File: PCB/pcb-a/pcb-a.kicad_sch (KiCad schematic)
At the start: 12 parts, among them Q3 BC337, SW1 config, U1 ESP32-S2-DevKitM

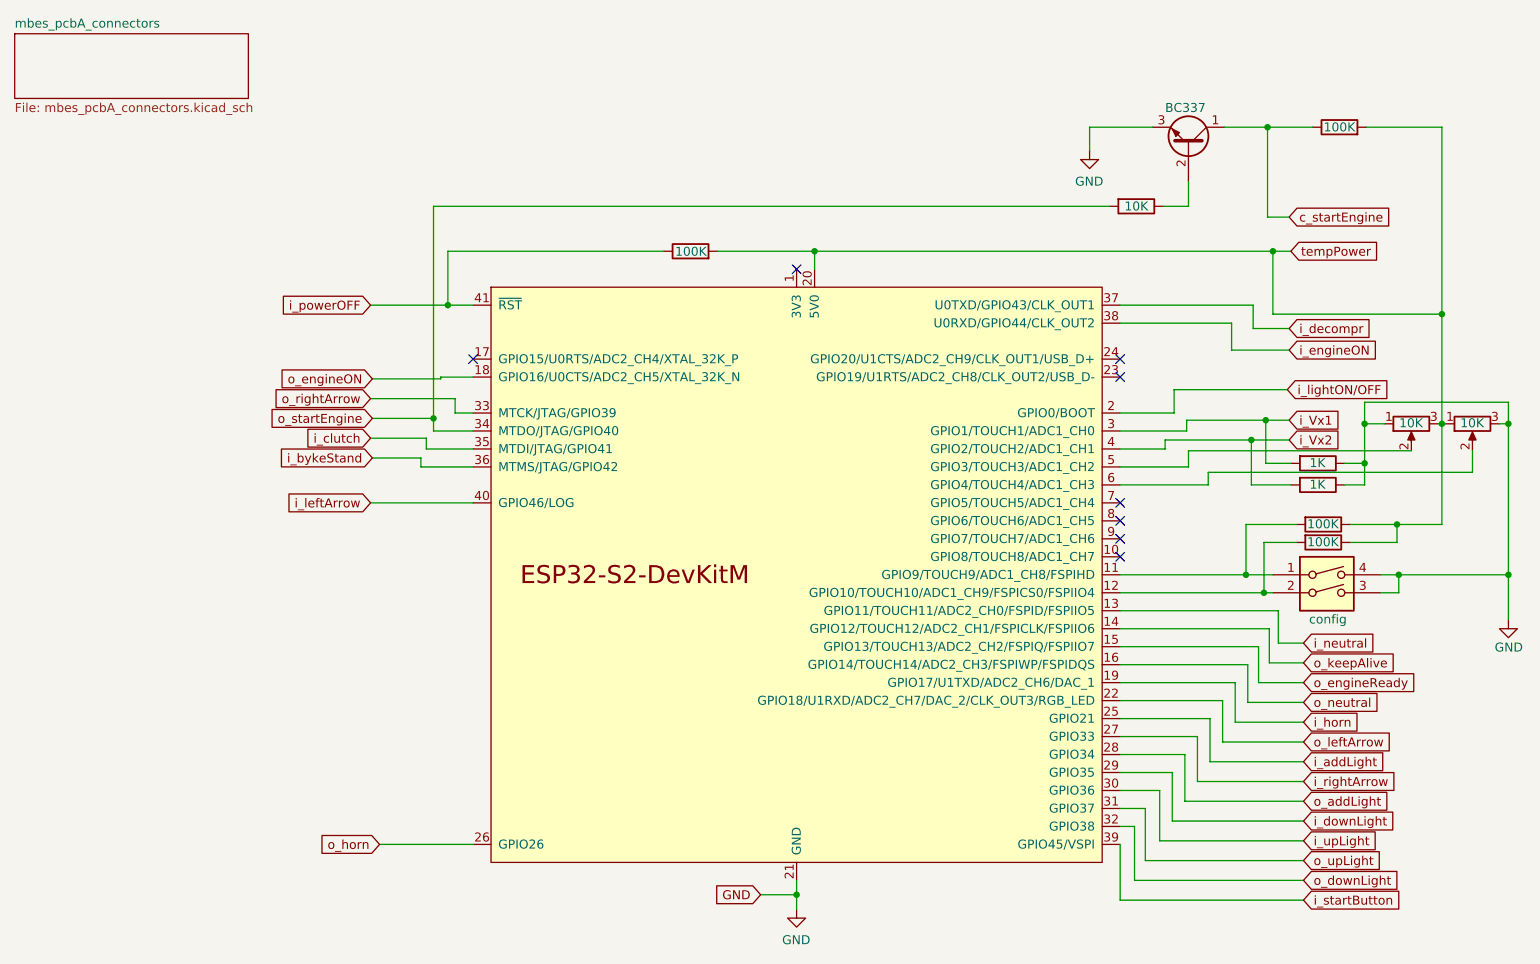
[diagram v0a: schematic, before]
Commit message: Fixes and updates
This version will be tested soon. It is fully implemented with THT devices using ESP32-S2 DevKit
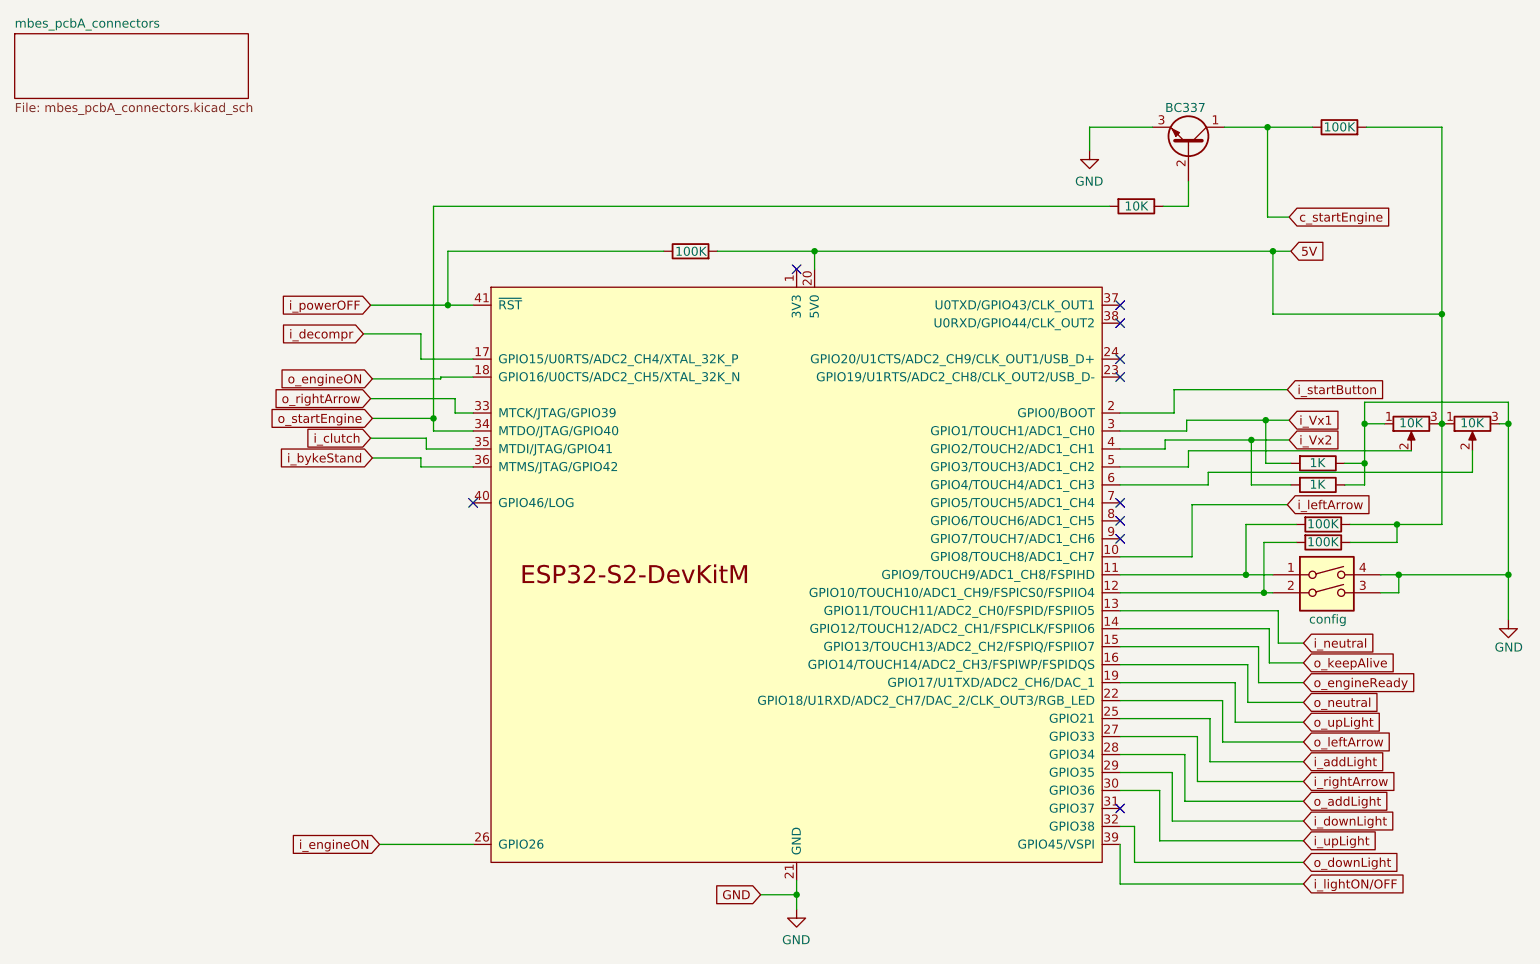
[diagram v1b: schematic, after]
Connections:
- net i_horn is gone; now on net o_upLight: U1.19 (GPIO17/U1TXD/ADC2_CH6/DAC_1)
- net o_horn is gone; now on net i_engineON: U1.26 (GPIO26)
- net i_decompr: now also U1.17 (GPIO15/U0RTS/ADC2_CH4/XTAL_32K_P); no longer U1.37 (U0TXD/GPIO43/CLK_OUT1)
- net i_engineON: no longer U1.38 (U0RXD/GPIO44/CLK_OUT2)
- net i_leftArrow: now also U1.10 (GPIO8/TOUCH8/ADC1_CH7); no longer U1.40 (GPIO46/LOG)
- net i_lightON/OFF: now also U1.39 (GPIO45/VSPI); no longer U1.2 (GPIO0/BOOT)
- net i_startButton: now also U1.2 (GPIO0/BOOT); no longer U1.39 (GPIO45/VSPI)
- net o_upLight: no longer U1.31 (GPIO37)
- net tempPower renamed 5V
- no-connect marks 8 -> 10

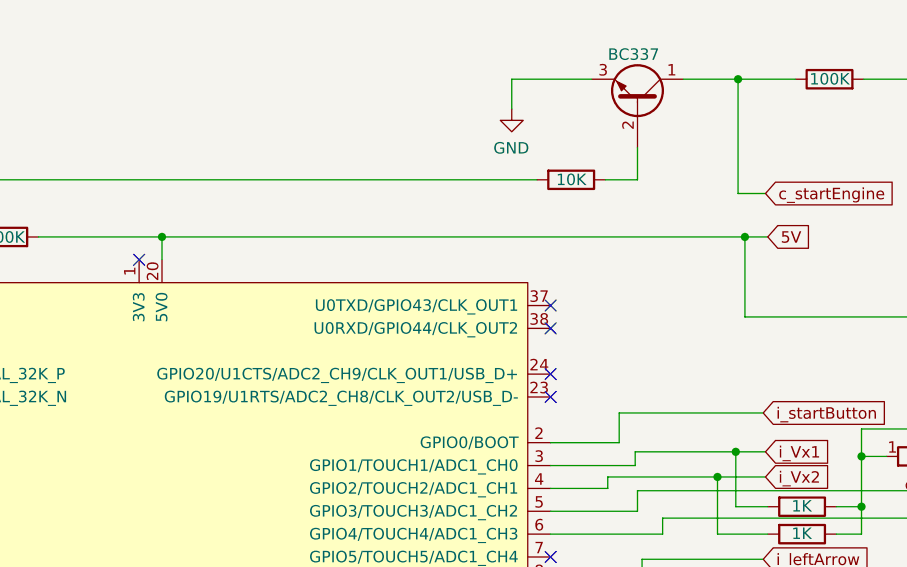
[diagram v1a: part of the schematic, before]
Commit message: Changes to reduce PCB size
- The resistors type has been changed from THT to SMD
- Configuration switches has been moved to fit PCB space in better way
- An electrolitic capicitor has been added
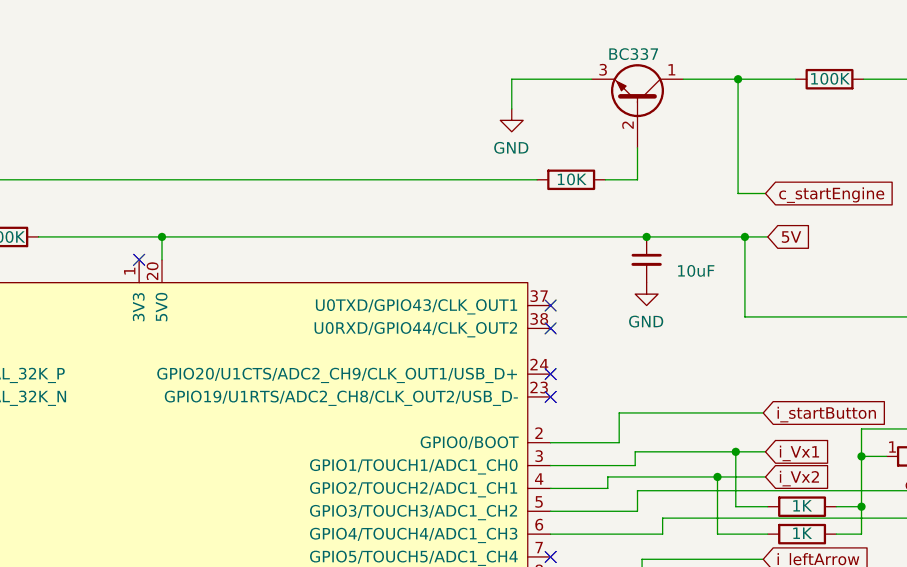
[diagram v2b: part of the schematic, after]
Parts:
- added C1: 10uF, Capacitor_THT:CP_Radial_D6.3mm_P2.50mm, symbol Device:C_Small
- R2, R3, R4, R5, R6, R7, R8: footprint Resistor_THT:R_Axial_DIN0204_L3.6mm_D1.6mm_P5.08mm_Horizontal -> Resistor_SMD:R_1206_3216Metric
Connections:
- net 5V: now also C1.1
- net GND: now also C1.2
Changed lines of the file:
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@@
 	)
 	(junction
+		(at 188.976 50.8)
+		(diameter 0)
+		(color 0 0 0 0)
+	)
+	(junction
 		(at 217.424 89.408)
 		(diameter 0)
@@
 	(wire
 		(pts
+			(xy 188.976 50.8) (xy 135.128 50.8)
+		)
+		(stroke
+			(width 0)
+			(type default)
+		)
+	)
+	(wire
+		(pts
 			(xy 199.39 104.14) (xy 178.308 104.14)
 		)
@@
 	(wire
 		(pts
-			(xy 199.898 50.8) (xy 135.128 50.8)
+			(xy 199.898 50.8) (xy 188.976 50.8)
 		)
 		(stroke
@@
 			)
 		)
-		(property "Footprint" "Resistor_THT:R_Axial_DIN0204_L3.6mm_D1.6mm_P5.08mm_Horizontal"
+		(property "Footprint" "Resistor_SMD:R_1206_3216Metric"
 			(at 206.248 82.042 90)
 			(effects
@@
 			)
 		)
-		(property "Footprint" "Resistor_THT:R_Axial_DIN0204_L3.6mm_D1.6mm_P5.08mm_Horizontal"
+		(property "Footprint" "Resistor_SMD:R_1206_3216Metric"
 			(at 206.248 78.994 90)
 			(effects
@@
 			)
 		)
-		(property "Footprint" "Resistor_THT:R_Axial_DIN0204_L3.6mm_D1.6mm_P5.08mm_Horizontal"
+		(property "Footprint" "Resistor_SMD:R_1206_3216Metric"
 			(at 207.01 87.63 90)
 			(effects
@@
 			)
 		)
-		(property "Footprint" "Resistor_THT:R_Axial_DIN0204_L3.6mm_D1.6mm_P5.08mm_Horizontal"
+		(property "Footprint" "Resistor_SMD:R_1206_3216Metric"
 			(at 207.01 90.17 90)
 			(effects
@@
 	)
 	(symbol
+		(lib_id "Device:C_Small")
+		(at 188.976 53.34 0)
+		(unit 1)
+		(exclude_from_sim no)
+		(in_bom yes)
+		(on_board yes)
+		(dnp no)
+		(fields_autoplaced yes)
+		(property "Reference" "C1"
+			(at 192.278 52.0762 0)
+			(effects
+				(font
+					(size 1.27 1.27)
+				)
+				(justify left)
+				(hide yes)
+			)
+		)
+		(property "Value" "10uF"
+			(at 192.278 54.6162 0)
+			(effects
+				(font
+					(size 1.27 1.27)
+				)
+				(justify left)
+			)
+		)
+		(property "Footprint" "Capacitor_THT:CP_Radial_D6.3mm_P2.50mm"
+			(at 188.976 53.34 0)
+			(effects
+				(font
+					(size 1.27 1.27)
+				)
+				(hide yes)
+			)
+		)
+		(property "Datasheet" "~"
+			(at 188.976 53.34 0)
+			(effects
+				(font
+					(size 1.27 1.27)
+				)
+				(hide yes)
+			)
+		)
+		(property "Description" "Unpolarized capacitor, small symbol"
+			(at 188.976 53.34 0)
+			(effects
+				(font
+					(size 1.27 1.27)
+				)
+				(hide yes)
+			)
+		)
+		(pin "2"
+		)
+		(pin "1"
+		)
+		(instances
+			(project ""
+				(path "/709d0967-afe5-49d3-92a5-d2bb94550bdb"
+					(reference "C1")
+					(unit 1)
+				)
+			)
+		)
+	)
+	(symbol
 		(lib_id "power:GND")
 		(at 173.99 36.576 0)
@@
 			)
 		)
-		(property "Footprint" "Resistor_THT:R_Axial_DIN0204_L3.6mm_D1.6mm_P5.08mm_Horizontal"
+		(property "Footprint" "Resistor_SMD:R_1206_3216Metric"
 			(at 180.594 42.672 90)
 			(effects
@@
 			)
 		)
-		(property "Footprint" "Resistor_THT:R_Axial_DIN0204_L3.6mm_D1.6mm_P5.08mm_Horizontal"
+		(property "Footprint" "Resistor_SMD:R_1206_3216Metric"
 			(at 117.602 52.578 90)
 			(effects
@@
 			)
 		)
-		(property "Footprint" "Resistor_THT:R_Axial_DIN0204_L3.6mm_D1.6mm_P5.08mm_Horizontal"
+		(property "Footprint" "Resistor_SMD:R_1206_3216Metric"
 			(at 209.296 35.052 90)
 			(effects
@@
 					(unit 1)
 				)
+			)
+		)
+	)
+	(symbol
+		(lib_id "power:GND")
+		(at 188.976 55.88 0)
+		(unit 1)
+		(exclude_from_sim no)
+		(in_bom yes)
+		(on_board yes)
+		(dnp no)
+		(property "Reference" "#PWR02"
+			(at 188.976 62.23 0)
+			(effects
+				(font
+					(size 1.27 1.27)
+				)
+				(hide yes)
+			)
+		)
+		(property "Value" "GND"
+			(at 188.9252 60.2488 0)
+			(effects
+				(font
+					(size 1.27 1.27)
+				)
+			)
+		)
+		(property "Footprint" ""
+			(at 188.976 55.88 0)
+			(effects
+				(font
+					(size 1.27 1.27)
+				)
+				(hide yes)
+			)
+		)
+		(property "Datasheet" ""
+			(at 188.976 55.88 0)
+			(effects
+				(font
+					(size 1.27 1.27)
+				)
+				(hide yes)
+			)
+		)
+		(property "Description" ""
+			(at 188.976 55.88 0)
+			(effects
+				(font
+					(size 1.27 1.27)
+				)
+				(hide yes)
+			)
+		)
+		(pin "1"
+		)
+		(instances
+			(project "pcb-a"
+				(path "/709d0967-afe5-49d3-92a5-d2bb94550bdb"
+					(reference "#PWR02")
+					(unit 1)
+				)

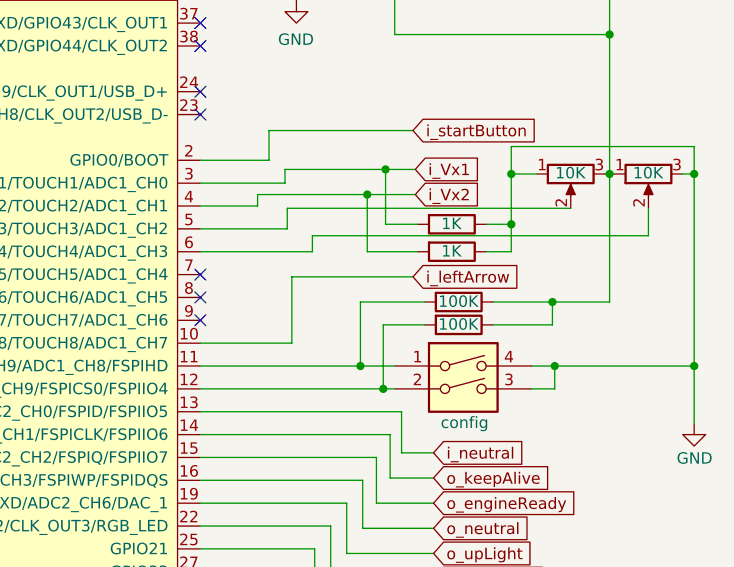
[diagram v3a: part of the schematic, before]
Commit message: hanges and fix
- The R6 and R8 pull-up resistors have been removed. I will use internal ones
- The J2 connector position has been moved
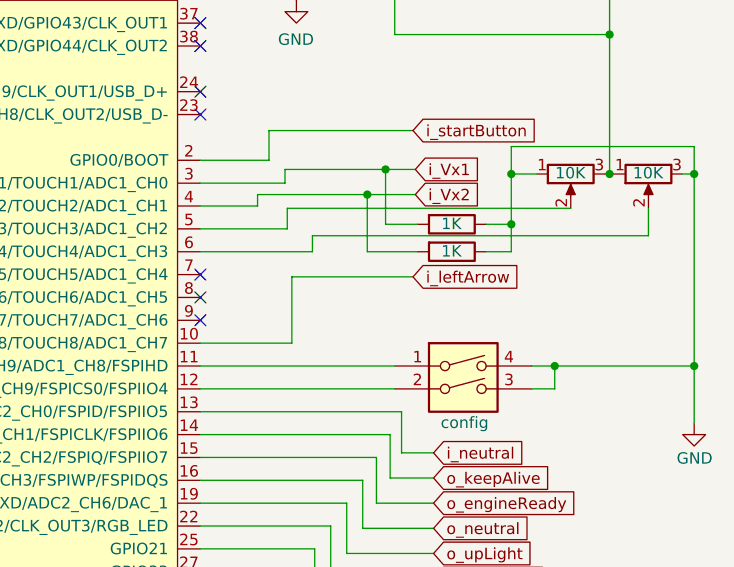
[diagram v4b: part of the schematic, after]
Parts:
- removed R5, R8: 100K, Resistor_SMD:R_1206_3216Metric, symbol Device:R

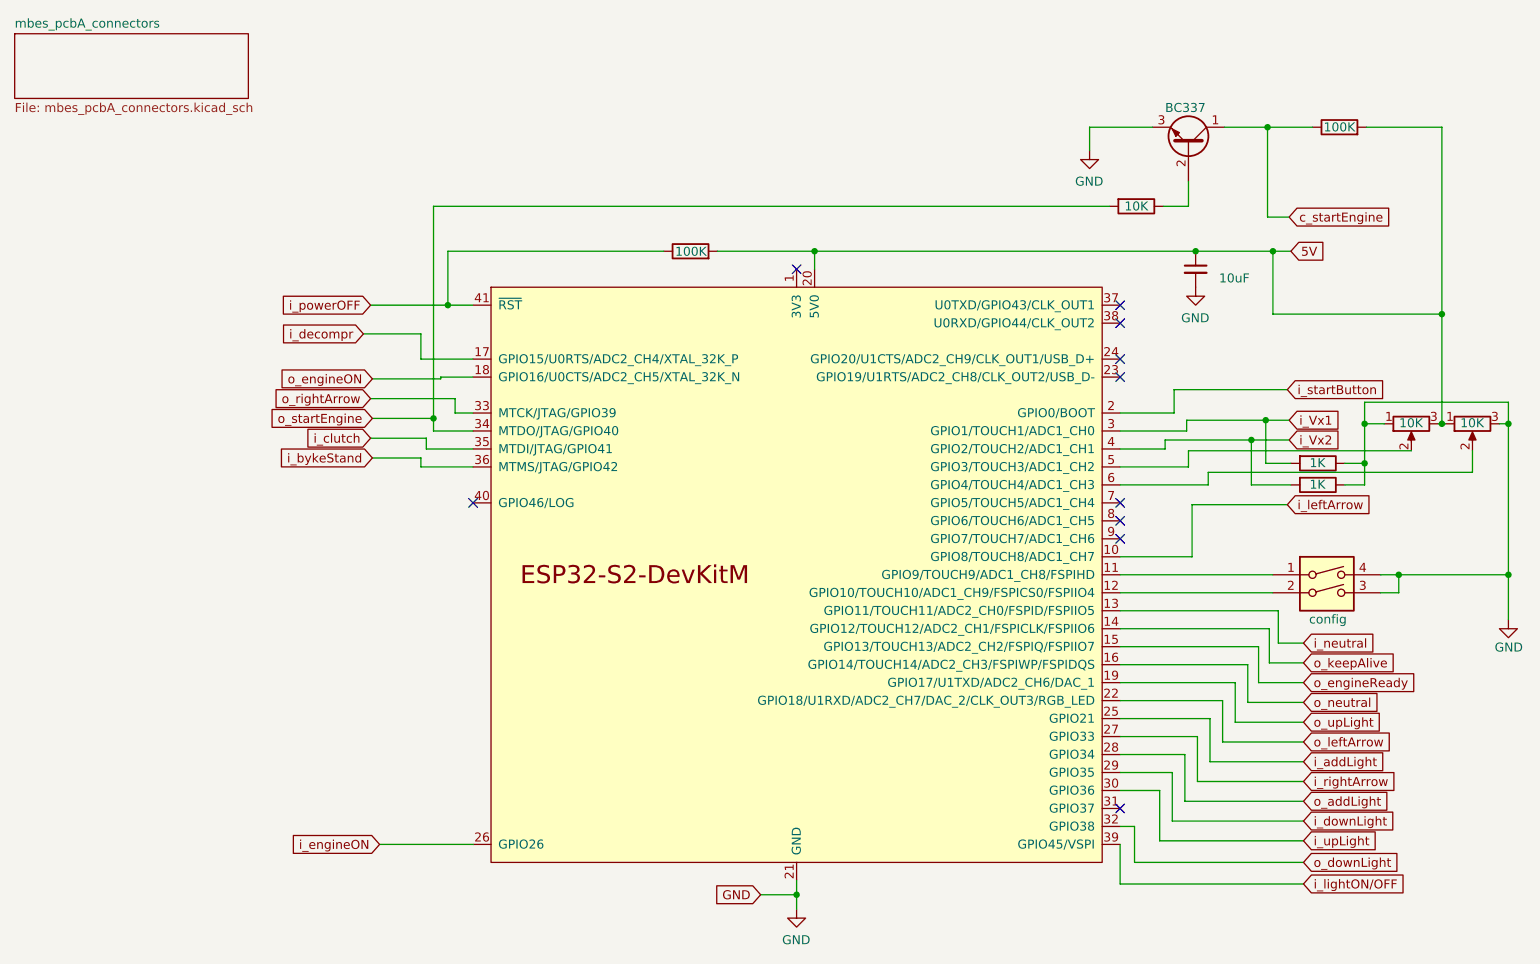
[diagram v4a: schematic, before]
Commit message: Communication with the rear power stage has been changed
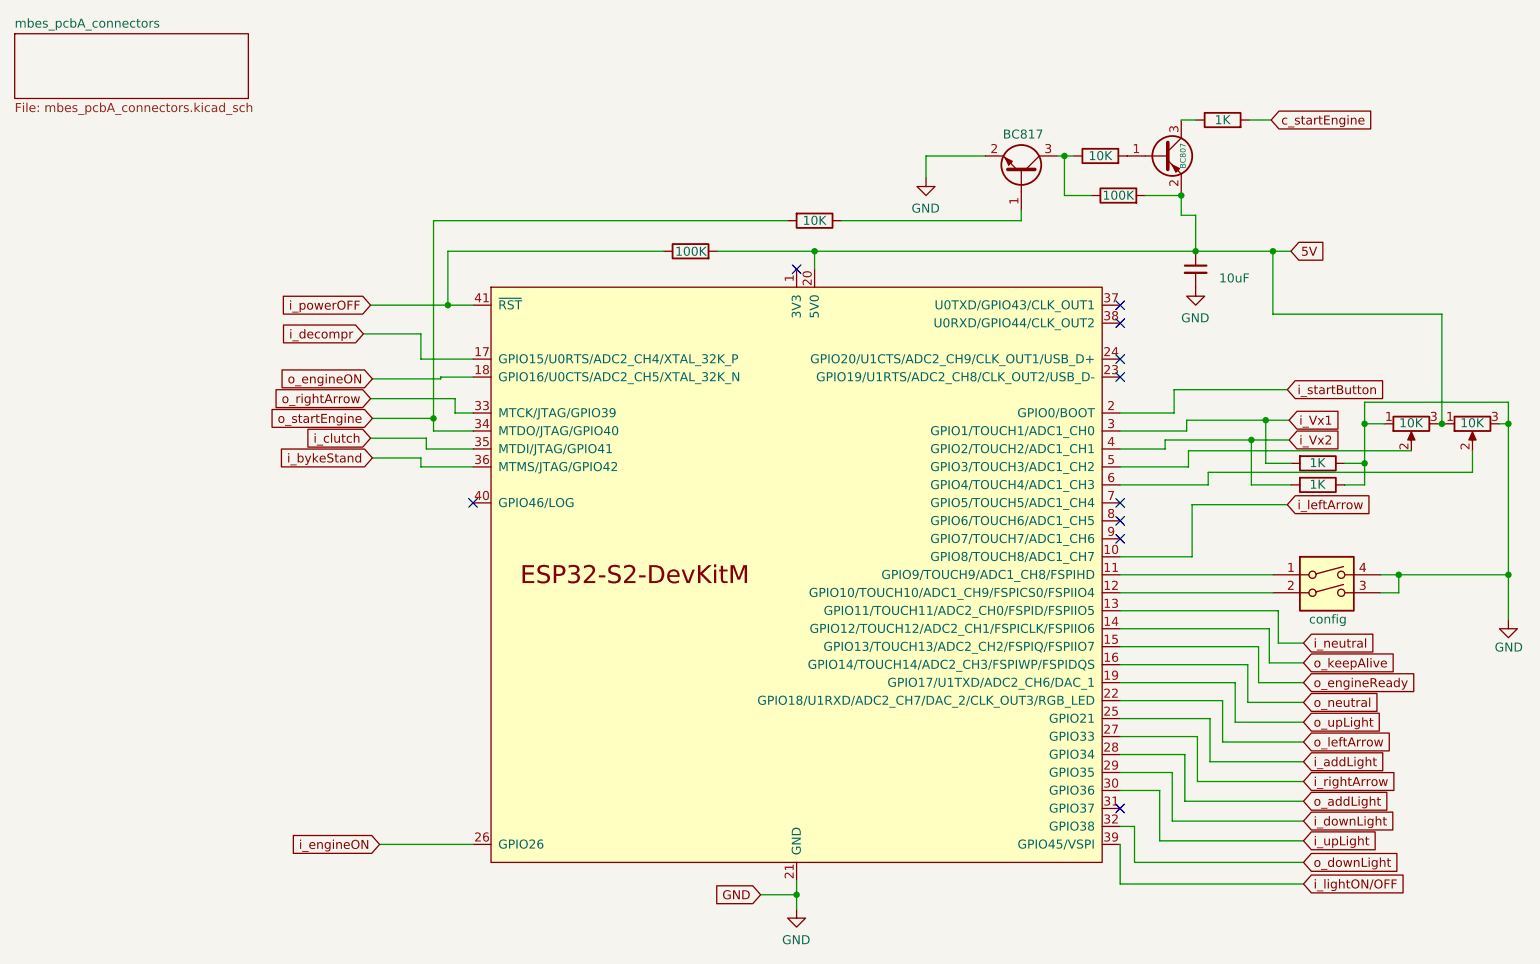
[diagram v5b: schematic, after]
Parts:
- removed Q3: BC337, Package_TO_SOT_THT:TO-92_Inline_Wide, symbol Transistor_BJT:BC337
- added Q1: BC807, Package_TO_SOT_SMD:SOT-23, symbol Transistor_BJT:BC807
- added Q3: BC817, Package_TO_SOT_SMD:SOT-23, symbol Transistor_BJT:BC817
- added R10: 10K, Resistor_SMD:R_1206_3216Metric, symbol Device:R
- added R15: 1K, Resistor_SMD:R_1206_3216Metric, symbol Device:R
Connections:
- net 5V: now also Q1.2 (E)
- net GND: now also Q3.2 (E)
- net c_startEngine: now also R15.2; no longer R6.1
- net at R7.1: now also Q3.1 (B)
- new net: Q1.1 (B), R10.2
- new net: Q1.3 (C), R15.1
- new net: Q3.3 (C), R10.1, R6.1
